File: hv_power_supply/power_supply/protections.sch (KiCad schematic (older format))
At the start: 50 parts, among them J6 CONN_01x02, K1 CPC1979J, Q2 SSM3K333R, Q3 SSM3K333R, Q4 FQD2N60CTM, U10 LT-1997-2, U11 ADA4661-2, U7 CPC1117NTR, U8 ACPL-C79B-500E, U9 ACPL-C87B-000E

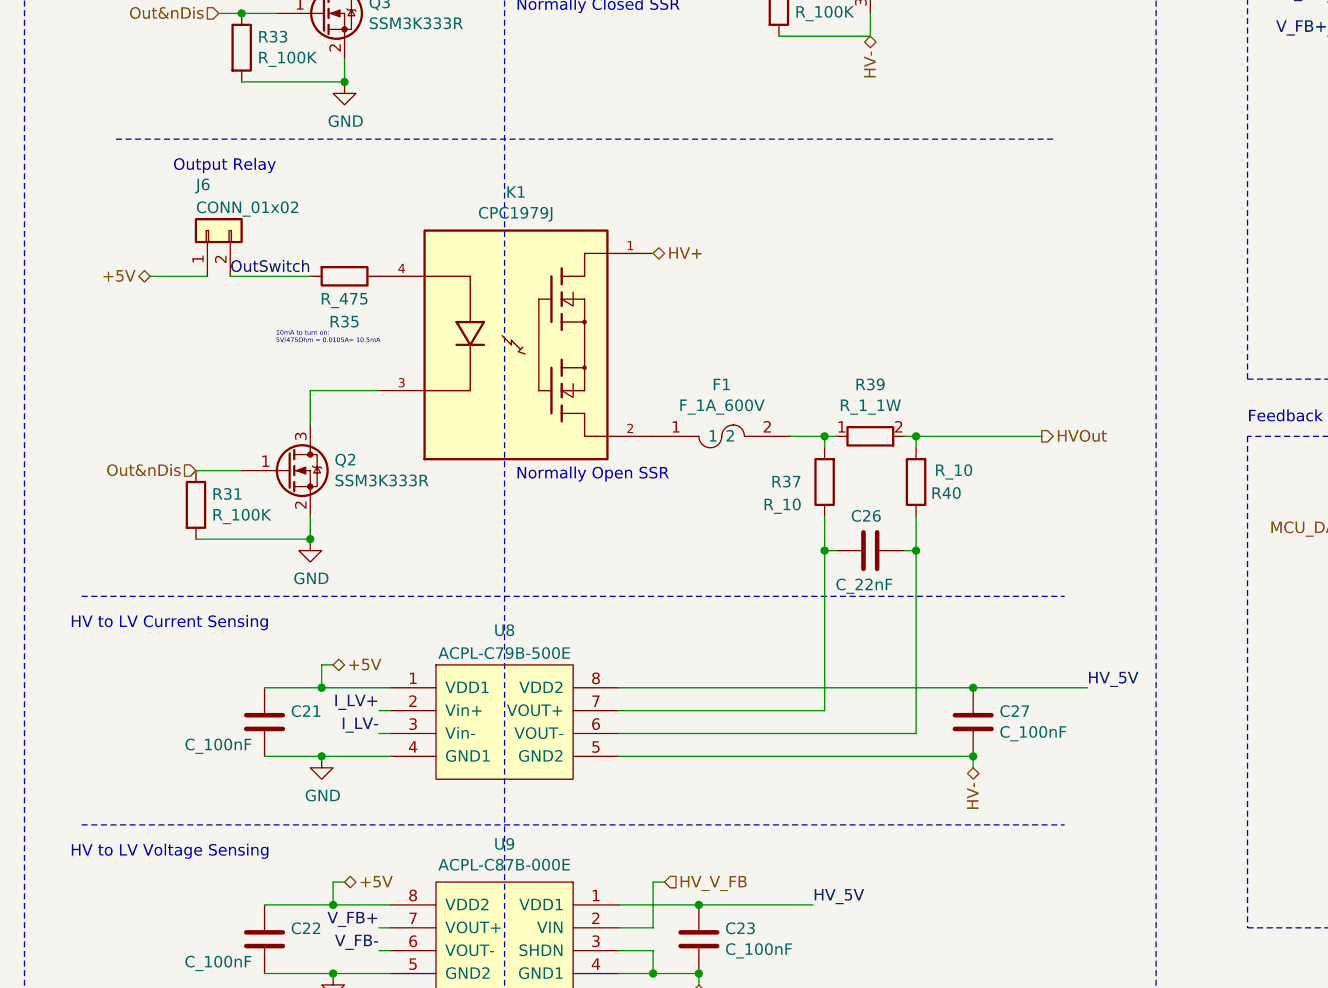
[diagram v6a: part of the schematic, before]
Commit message: Most of placement done, beginning routing.
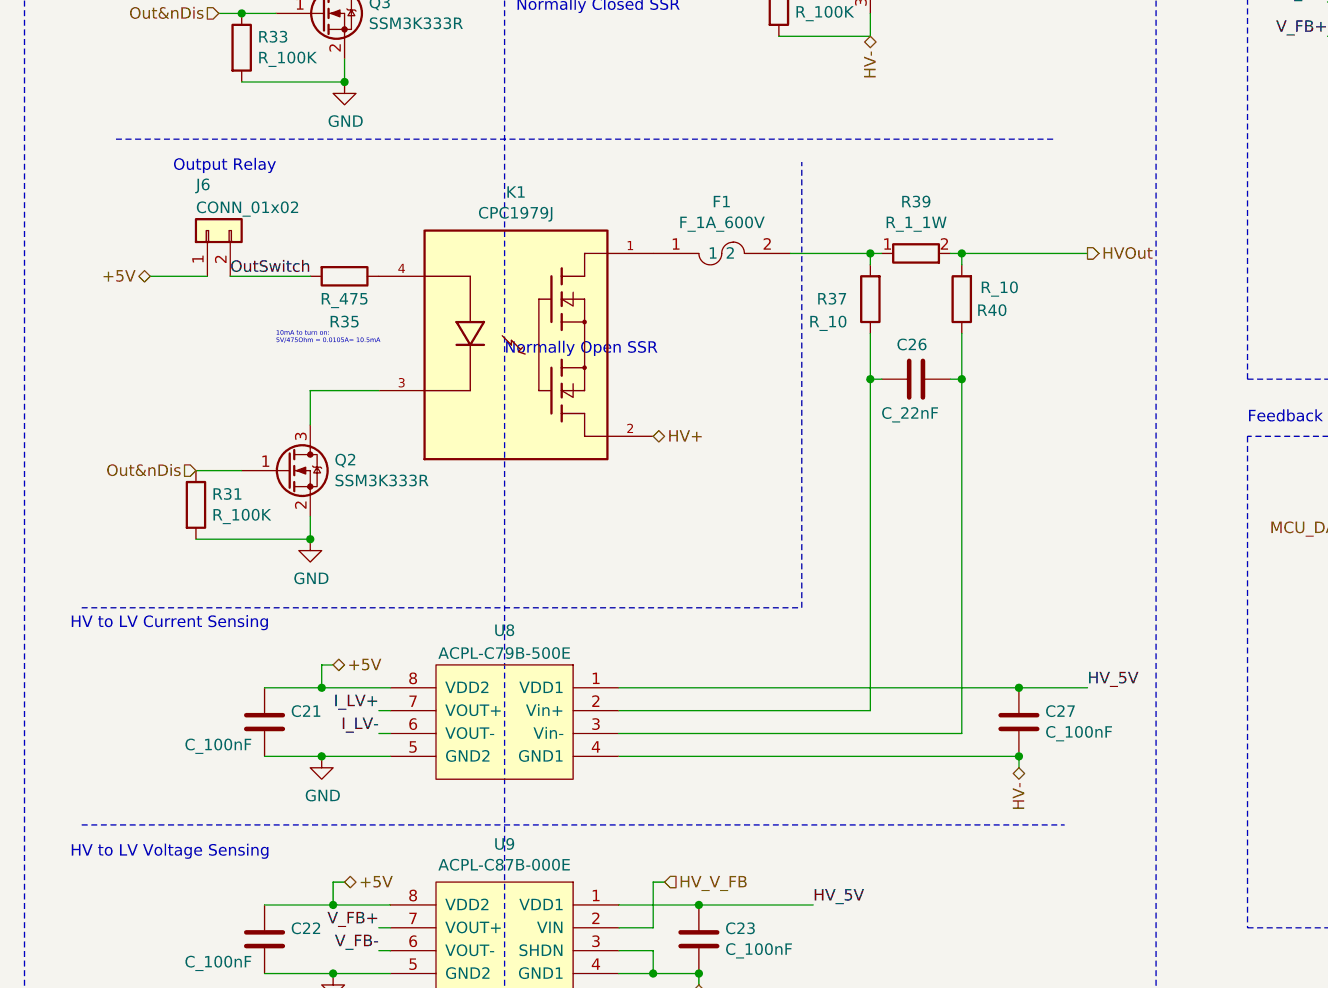
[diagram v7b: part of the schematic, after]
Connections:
- net +5V: now also U8.8 (VDD2); no longer U8.1 (VDD1)
- net GND: now also U8.5 (GND2); no longer U8.4 (GND1)
- net HV+: now also K1.2; no longer K1.1
- net HV-: now also U8.4 (GND1); no longer U8.5 (GND2)
- net HV_5V: now also U8.1 (VDD1); no longer U8.8 (VDD2)
- net I_LV+: now also U8.7 (VOUT+); no longer U8.2 (Vin+)
- net I_LV-: now also U8.6 (VOUT-); no longer U8.3 (Vin-)
- net at F1.1: now also K1.1; no longer K1.2
- net at C26.1, R37.1: now also U8.2 (Vin+); no longer U8.7 (VOUT+)
- net at C26.2, R40.1: now also U8.3 (Vin-); no longer U8.6 (VOUT-)
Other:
- moved on the sheet: C26, C27, F1, R37, R39, R40
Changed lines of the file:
@@
 Wire Wire Line
 	1800 3800 2100 3800
-Text HLabel 3300 3200 2    50   BiDi ~ 0
+Text HLabel 3300 4000 2    50   BiDi ~ 0
 HV+
-Text HLabel 5000 4000 2    50   Output ~ 0
+Text HLabel 5200 3200 2    50   Output ~ 0
 HVOut
-Text Notes 2700 4200 0    50   ~ 0
+Text Notes 2650 3650 0    50   ~ 0
 Normally Open SSR
 $Comp
 L formula:F_1A_600V F1
 U 1 1 60398FFC
-P 3600 4000
-F 0 "F1" H 3600 4225 50  0000 C CNN
-F 1 "F_1A_600V" H 3600 4134 50  0000 C CNN
-F 2 "footprints:Fuse_1A_600V" H 3600 3700 50  0001 C CNN
-F 3 "https://media.digikey.com/pdf/Data%20Sheets/Bel%20Fuse%20PDFs/0ADAC_0ADAP_Series.pdf" H 3550 4000 50  0001 C CNN
-F 4 "https://www.digikey.com/product-detail/en/bel-fuse-inc/0ADAP1000-RE/507-2220-ND/8028479" H 3800 4350 50  0001 C CNN "PurchasingLink"
-	1    3600 4000
+P 3600 3200
+F 0 "F1" H 3600 3425 50  0000 C CNN
+F 1 "F_1A_600V" H 3600 3334 50  0000 C CNN
+F 2 "footprints:Fuse_1A_600V" H 3600 2900 50  0001 C CNN
+F 3 "https://media.digikey.com/pdf/Data%20Sheets/Bel%20Fuse%20PDFs/0ADAC_0ADAP_Series.pdf" H 3550 3200 50  0001 C CNN
+F 4 "https://www.digikey.com/product-detail/en/bel-fuse-inc/0ADAP1000-RE/507-2220-ND/8028479" H 3800 3550 50  0001 C CNN "PurchasingLink"
+	1    3600 3200
 	1    0    0    -1
 $EndComp
@@
 F 6 "https://www.digikey.com/en/products/detail/broadcom-limited/ACPL-C79B-500E/2347208" H 2650 6300 50  0001 C CNN "Purchasing Link"
 	1    2650 5500
-	1    0    0    -1
+	-1   0    0    -1
 $EndComp
 Wire Wire Line
@@
 	1    0    0    -1
 $EndComp
-Wire Wire Line
-	4700 5100 5200 5100
 $Comp
 L formula:C_100nF C27
 U 1 1 60FD25AC
-P 4700 5250
-F 0 "C27" H 4815 5296 50  0000 L CNN
-F 1 "C_100nF" H 4815 5205 50  0000 L CNN
-F 2 "footprints:C_0603_1608Metric" H 4738 5100 50  0001 C CNN
-F 3 "http://www.samsungsem.com/kr/support/product-search/mlcc/CL10A475KQ8NNNC.jsp" H 4725 5350 50  0001 C CNN
-F 4 "DK" H 4700 5250 60  0001 C CNN "MFN"
-F 5 "1276-6717-1-ND" H 4700 5250 60  0001 C CNN "MPN"
-F 6 "https://www.digikey.com/product-detail/en/samsung-electro-mechanics/CL10B104KA8WPNC/1276-6717-1-ND/5961576" H 5125 5750 60  0001 C CNN "PurchasingLink"
-	1    4700 5250
+P 4900 5250
+F 0 "C27" H 5015 5296 50  0000 L CNN
+F 1 "C_100nF" H 5015 5205 50  0000 L CNN
+F 2 "footprints:C_0603_1608Metric" H 4938 5100 50  0001 C CNN
+F 3 "http://www.samsungsem.com/kr/support/product-search/mlcc/CL10A475KQ8NNNC.jsp" H 4925 5350 50  0001 C CNN
+F 4 "DK" H 4900 5250 60  0001 C CNN "MFN"
+F 5 "1276-6717-1-ND" H 4900 5250 60  0001 C CNN "MPN"
+F 6 "https://www.digikey.com/product-detail/en/samsung-electro-mechanics/CL10B104KA8WPNC/1276-6717-1-ND/5961576" H 5325 5750 60  0001 C CNN "PurchasingLink"
+	1    4900 5250
 	1    0    0    -1
 $EndComp
@@
 L formula:R_10 R40
 U 1 1 60FD2651
-P 4450 4200
-F 0 "R40" H 4250 4250 50  0000 L CNN
-F 1 "R_10" H 4200 4150 50  0000 L CNN
-F 2 "footprints:R_0805_OEM" H 4380 4200 50  0001 C CNN
-F 3 "" H 4530 4200 50  0001 C CNN
-F 4 "Panasonic Electronic Components" H 4450 4200 60  0001 C CNN "MFN"
-F 5 "ERJ-P06F10R0V" H 4450 4200 60  0001 C CNN "MPN"
-F 6 "https://www.digikey.com/en/products/detail/panasonic-electronic-components/ERJ-P06F10R0V/5722444" H 4930 4600 60  0001 C CNN "PurchasingLink"
-	1    4450 4200
+P 4650 3400
+F 0 "R40" H 4450 3450 50  0000 L CNN
+F 1 "R_10" H 4400 3350 50  0000 L CNN
+F 2 "footprints:R_0805_OEM" H 4580 3400 50  0001 C CNN
+F 3 "" H 4730 3400 50  0001 C CNN
+F 4 "Panasonic Electronic Components" H 4650 3400 60  0001 C CNN "MFN"
+F 5 "ERJ-P06F10R0V" H 4650 3400 60  0001 C CNN "MPN"
+F 6 "https://www.digikey.com/en/products/detail/panasonic-electronic-components/ERJ-P06F10R0V/5722444" H 5130 3800 60  0001 C CNN "PurchasingLink"
+	1    4650 3400
 	-1   0    0    1
 $EndComp
@@
 L formula:R_10 R37
 U 1 1 60FD265A
-P 4050 4200
-F 0 "R37" H 4150 4200 50  0000 L CNN
-F 1 "R_10" H 4150 4300 50  0000 L CNN
-F 2 "footprints:R_0805_OEM" H 3980 4200 50  0001 C CNN
-F 3 "" H 4130 4200 50  0001 C CNN
-F 4 "Panasonic Electronic Components" H 4050 4200 60  0001 C CNN "MFN"
-F 5 "ERJ-P06F10R0V" H 4050 4200 60  0001 C CNN "MPN"
-F 6 "https://www.digikey.com/en/products/detail/panasonic-electronic-components/ERJ-P06F10R0V/5722444" H 4530 4600 60  0001 C CNN "PurchasingLink"
-	1    4050 4200
+P 4250 3400
+F 0 "R37" H 4350 3400 50  0000 L CNN
+F 1 "R_10" H 4350 3500 50  0000 L CNN
+F 2 "footprints:R_0805_OEM" H 4180 3400 50  0001 C CNN
+F 3 "" H 4330 3400 50  0001 C CNN
+F 4 "Panasonic Electronic Components" H 4250 3400 60  0001 C CNN "MFN"
+F 5 "ERJ-P06F10R0V" H 4250 3400 60  0001 C CNN "MPN"
+F 6 "https://www.digikey.com/en/products/detail/panasonic-electronic-components/ERJ-P06F10R0V/5722444" H 4730 3800 60  0001 C CNN "PurchasingLink"
+	1    4250 3400
 	-1   0    0    1
 $EndComp
@@
 	3500 6400 3500 6350
 Connection ~ 3500 6350
-Text HLabel 4700 5450 3    50   BiDi ~ 0
+Text HLabel 4900 5450 3    50   BiDi ~ 0
 HV-
 Wire Wire Line
-	4700 5450 4700 5400
-Connection ~ 4700 5400
+	4900 5450 4900 5400
 Text HLabel 7700 4100 2    50   BiDi ~ 0
 +5V
@@
 L formula:C_22nF C26
 U 1 1 6075A2B6
-P 4250 4500
-F 0 "C26" V 4400 4450 50  0000 L CNN
-F 1 "C_22nF" V 4100 4400 50  0000 L CNN
-F 2 "footprints:C_0805_OEM" H 4288 4350 50  0001 C CNN
-F 3 "https://content.kemet.com/datasheets/KEM_C1091_C0G_ESD.pdf" H 4275 4600 50  0001 C CNN
-F 4 "KEMET" H 4250 4500 60  0001 C CNN "MFN"
-F 5 "C0805C223G3GEC7800" H 4250 4500 60  0001 C CNN "MPN"
-F 6 "https://www.digikey.com/en/products/detail/kemet/C0805C223G3GEC7800/8644469" H 4675 5000 60  0001 C CNN "PurchasingLink"
-	1    4250 4500
+P 4450 3750
+F 0 "C26" V 4600 3700 50  0000 L CNN
+F 1 "C_22nF" V 4300 3650 50  0000 L CNN
+F 2 "footprints:C_0805_OEM" H 4488 3600 50  0001 C CNN
+F 3 "https://content.kemet.com/datasheets/KEM_C1091_C0G_ESD.pdf" H 4475 3850 50  0001 C CNN
+F 4 "KEMET" H 4450 3750 60  0001 C CNN "MFN"
+F 5 "C0805C223G3GEC7800" H 4450 3750 60  0001 C CNN "MPN"
+F 6 "https://www.digikey.com/en/products/detail/kemet/C0805C223G3GEC7800/8644469" H 4875 4250 60  0001 C CNN "PurchasingLink"
+	1    4450 3750
 	0    -1   -1   0
 $EndComp
 Wire Wire Line
-	4100 4500 4050 4500
-Wire Wire Line
-	4400 4500 4450 4500
+	4300 3750 4250 3750
+Wire Wire Line
+	4600 3750 4650 3750
 $Comp
 L formula:R_1_1W R39
 U 1 1 610B8730
-P 4250 4000
-F 0 "R39" H 4250 4225 50  0000 C CNN
-F 1 "R_1_1W" H 4250 4134 50  0000 C CNN
-F 2 "formula:R_2512_LARGE" H 4150 3800 50  0001 C CNN
-F 3 "https://www.vishay.com/docs/20035/dcrcwe3.pdf" V 4250 4000 50  0001 C CNN
-F 4 "https://www.digikey.com/en/products/detail/vishay-dale/CRCW25121R00FNEG/1173515" H 4250 3750 50  0001 C CNN "Link"
-	1    4250 4000
+P 4450 3200
+F 0 "R39" H 4450 3425 50  0000 C CNN
+F 1 "R_1_1W" H 4450 3334 50  0000 C CNN
+F 2 "formula:R_2512_LARGE" H 4350 3000 50  0001 C CNN
+F 3 "https://www.vishay.com/docs/20035/dcrcwe3.pdf" V 4450 3200 50  0001 C CNN
+F 4 "https://www.digikey.com/en/products/detail/vishay-dale/CRCW25121R00FNEG/1173515" H 4450 2950 50  0001 C CNN "Link"
+	1    4450 3200
 	1    0    0    -1
 $EndComp
@@
 Wire Wire Line
 	1900 6050 2150 6050
-Wire Wire Line
-	3150 5400 4700 5400
-Wire Wire Line
-	3150 5100 4700 5100
-Connection ~ 4700 5100
 Wire Wire Line
 	9950 2900 10550 2900
@@
 Connection ~ 9950 2750
 Wire Wire Line
-	3900 4000 4050 4000
-Wire Wire Line
-	4400 4000 4450 4000
-Wire Wire Line
-	4050 4000 4050 4050
-Connection ~ 4050 4000
-Wire Wire Line
-	4050 4000 4100 4000
-Wire Wire Line
-	4450 4050 4450 4000
-Connection ~ 4450 4000
-Wire Wire Line
-	4450 4000 5000 4000
-Wire Wire Line
-	4050 4500 4050 4350
-Wire Wire Line
-	4450 4500 4450 4350
+	4600 3200 4650 3200
+Wire Wire Line
+	4250 3200 4250 3250
+Connection ~ 4250 3200
+Wire Wire Line
+	4250 3200 4300 3200
+Wire Wire Line
+	4650 3250 4650 3200
+Connection ~ 4650 3200
+Wire Wire Line
+	4650 3200 5200 3200
 Wire Wire Line
 	1100 7250 1150 7250
@@
 Wire Notes Line
 	950  2700 5050 2700
-Wire Notes Line
-	800  4700 5100 4700
 Wire Wire Line
 	3300 5950 3350 5950
@@
 Text Notes 750  4850 0    50   ~ 0
 HV to LV Current Sensing
-Wire Wire Line
-	4050 5200 4050 4500
-Wire Wire Line
-	3150 5200 4050 5200
-Connection ~ 4050 4500
-Wire Wire Line
-	4450 4500 4450 5300
-Wire Wire Line
-	3150 5300 4450 5300
-Connection ~ 4450 4500
+Connection ~ 4250 3750
 Text Notes 750  5850 0    50   ~ 0
 HV to LV Voltage Sensing
@@
 	0    -1   -1   0
 $EndComp
+Wire Wire Line
+	4250 3550 4250 3750
+Wire Wire Line
+	4650 3550 4650 3750
+Wire Wire Line
+	4250 3750 4250 5200
+Connection ~ 4650 3750
+Wire Wire Line
+	4650 3750 4650 5300
+Wire Notes Line
+	800  4750 3950 4750
+Wire Notes Line
+	3950 4750 3950 2800
+Connection ~ 4900 5100
+Wire Wire Line
+	4900 5100 5200 5100
+Wire Wire Line
+	3150 5100 4900 5100
+Wire Wire Line
+	3150 5400 4900 5400
+Connection ~ 4900 5400
+Wire Wire Line
+	3150 5300 4650 5300
+Wire Wire Line
+	3150 5200 4250 5200
+Wire Wire Line
+	3900 3200 4250 3200
 $EndSCHEMATC

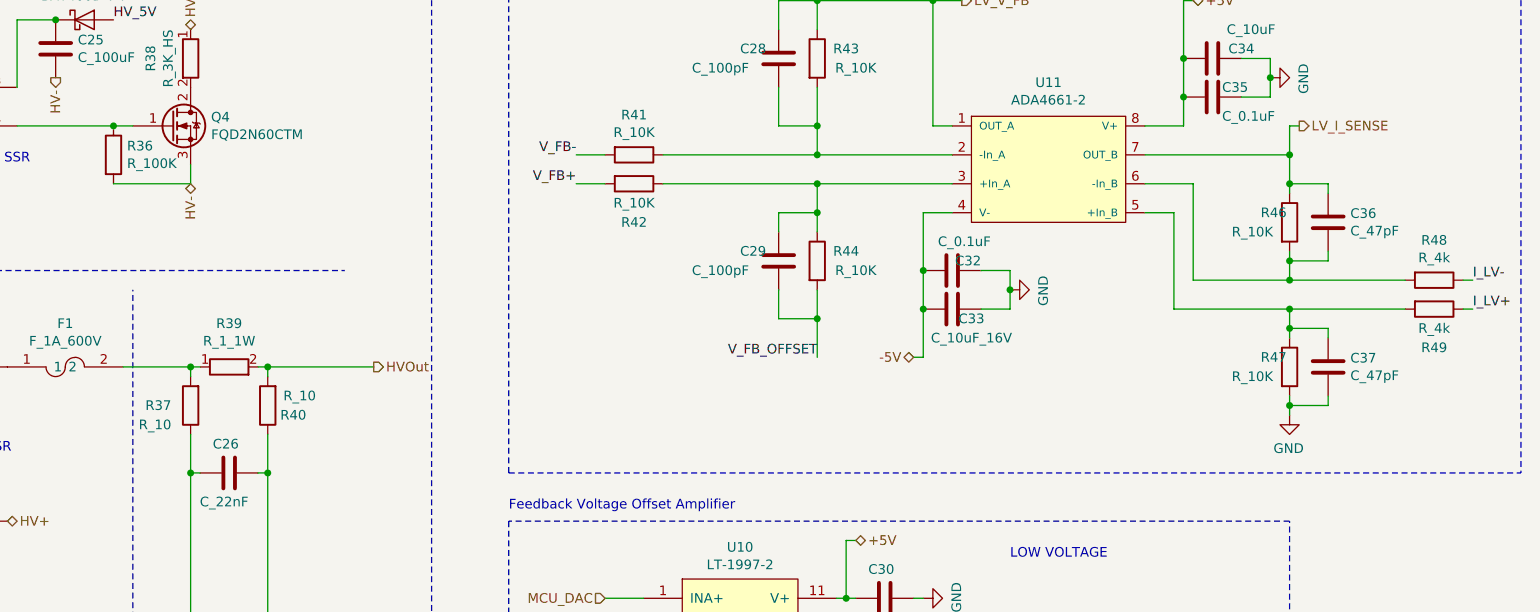
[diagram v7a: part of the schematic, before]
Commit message: All routing finished except for 5V and GND... Need to look into adding input filtering to power supply chips and some GND separation between LV, Flyback, and HV
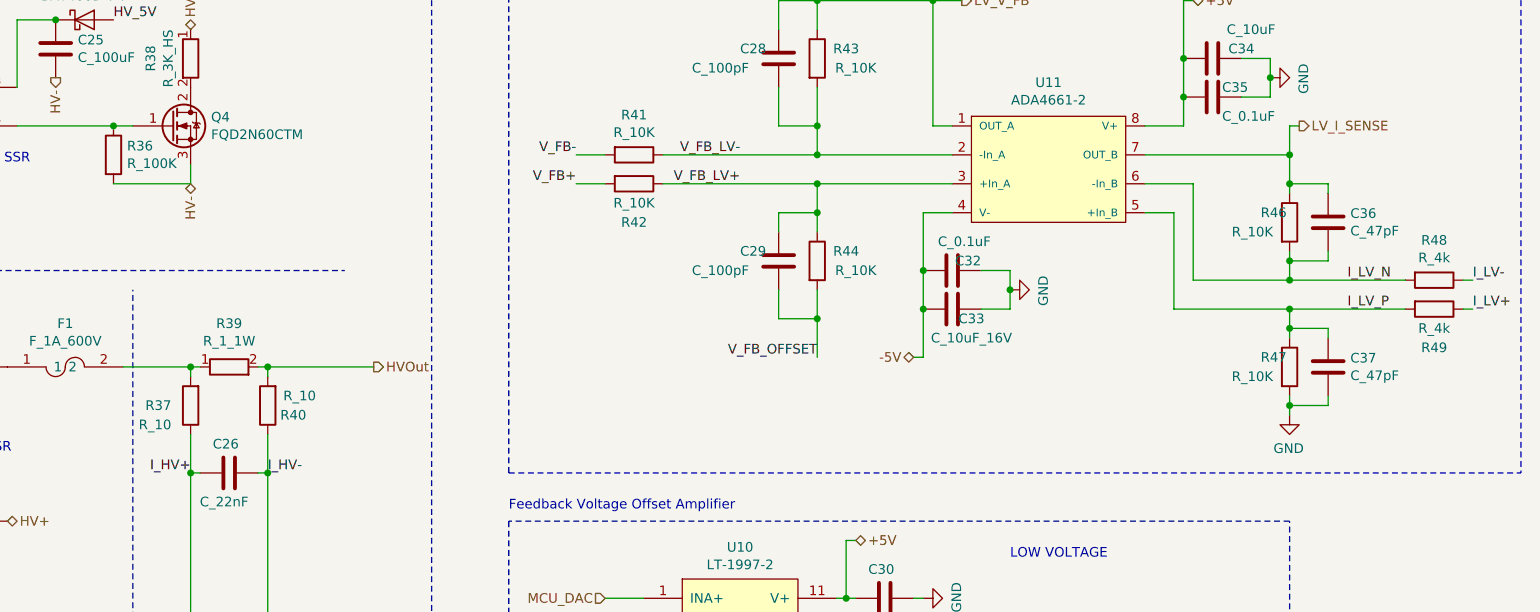
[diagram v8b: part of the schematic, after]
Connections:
- net I_HV+: now reaches C26.1, R37.1, U8.2 (Vin+)
- net I_HV-: now reaches C26.2, R40.1, U8.3 (Vin-)
- net V_FB_LV-: now reaches C28.2, R41.1, R43.2, U11.2 (-In_A)
- net V_FB_LV+: now reaches C29.1, R42.1, R44.1, U11.3 (+In_A)
- net I_LV_P: now reaches C37.1, R47.1, R49.2, U11.5 (+In_B)
- net I_LV_N: now reaches C36.2, R46.2, R48.2, U11.6 (-In_B)
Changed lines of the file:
@@
 Wire Wire Line
 	1900 6050 2150 6050
-Wire Wire Line
-	9950 2900 10550 2900
 Connection ~ 9950 2900
-Wire Wire Line
-	9950 2750 10550 2750
 Connection ~ 9950 2750
 Wire Wire Line
@@
 Wire Wire Line
 	3900 3200 4250 3200
+Text Label 4650 3750 0    50   ~ 0
+I_HV-
+Text Label 4250 3750 2    50   ~ 0
+I_HV+
+Text Label 7100 2250 2    50   ~ 0
+V_FB_LV+
+Text Label 7100 2100 2    50   ~ 0
+V_FB_LV-
+Text Label 10250 2750 0    50   ~ 0
+I_LV_N
+Text Label 10250 2900 0    50   ~ 0
+I_LV_P
+Wire Wire Line
+	9950 2900 10550 2900
+Wire Wire Line
+	9950 2750 10550 2750
 $EndSCHEMATC
